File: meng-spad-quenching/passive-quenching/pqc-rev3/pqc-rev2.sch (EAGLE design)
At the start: 61 parts, among them IC1 OPA858, IC2 OPA858, IC4 TPS7A4901, X1 CONN_SPAD, X2 PWR, X4 VBIAS_IN, X5 SIGNAL_OUT

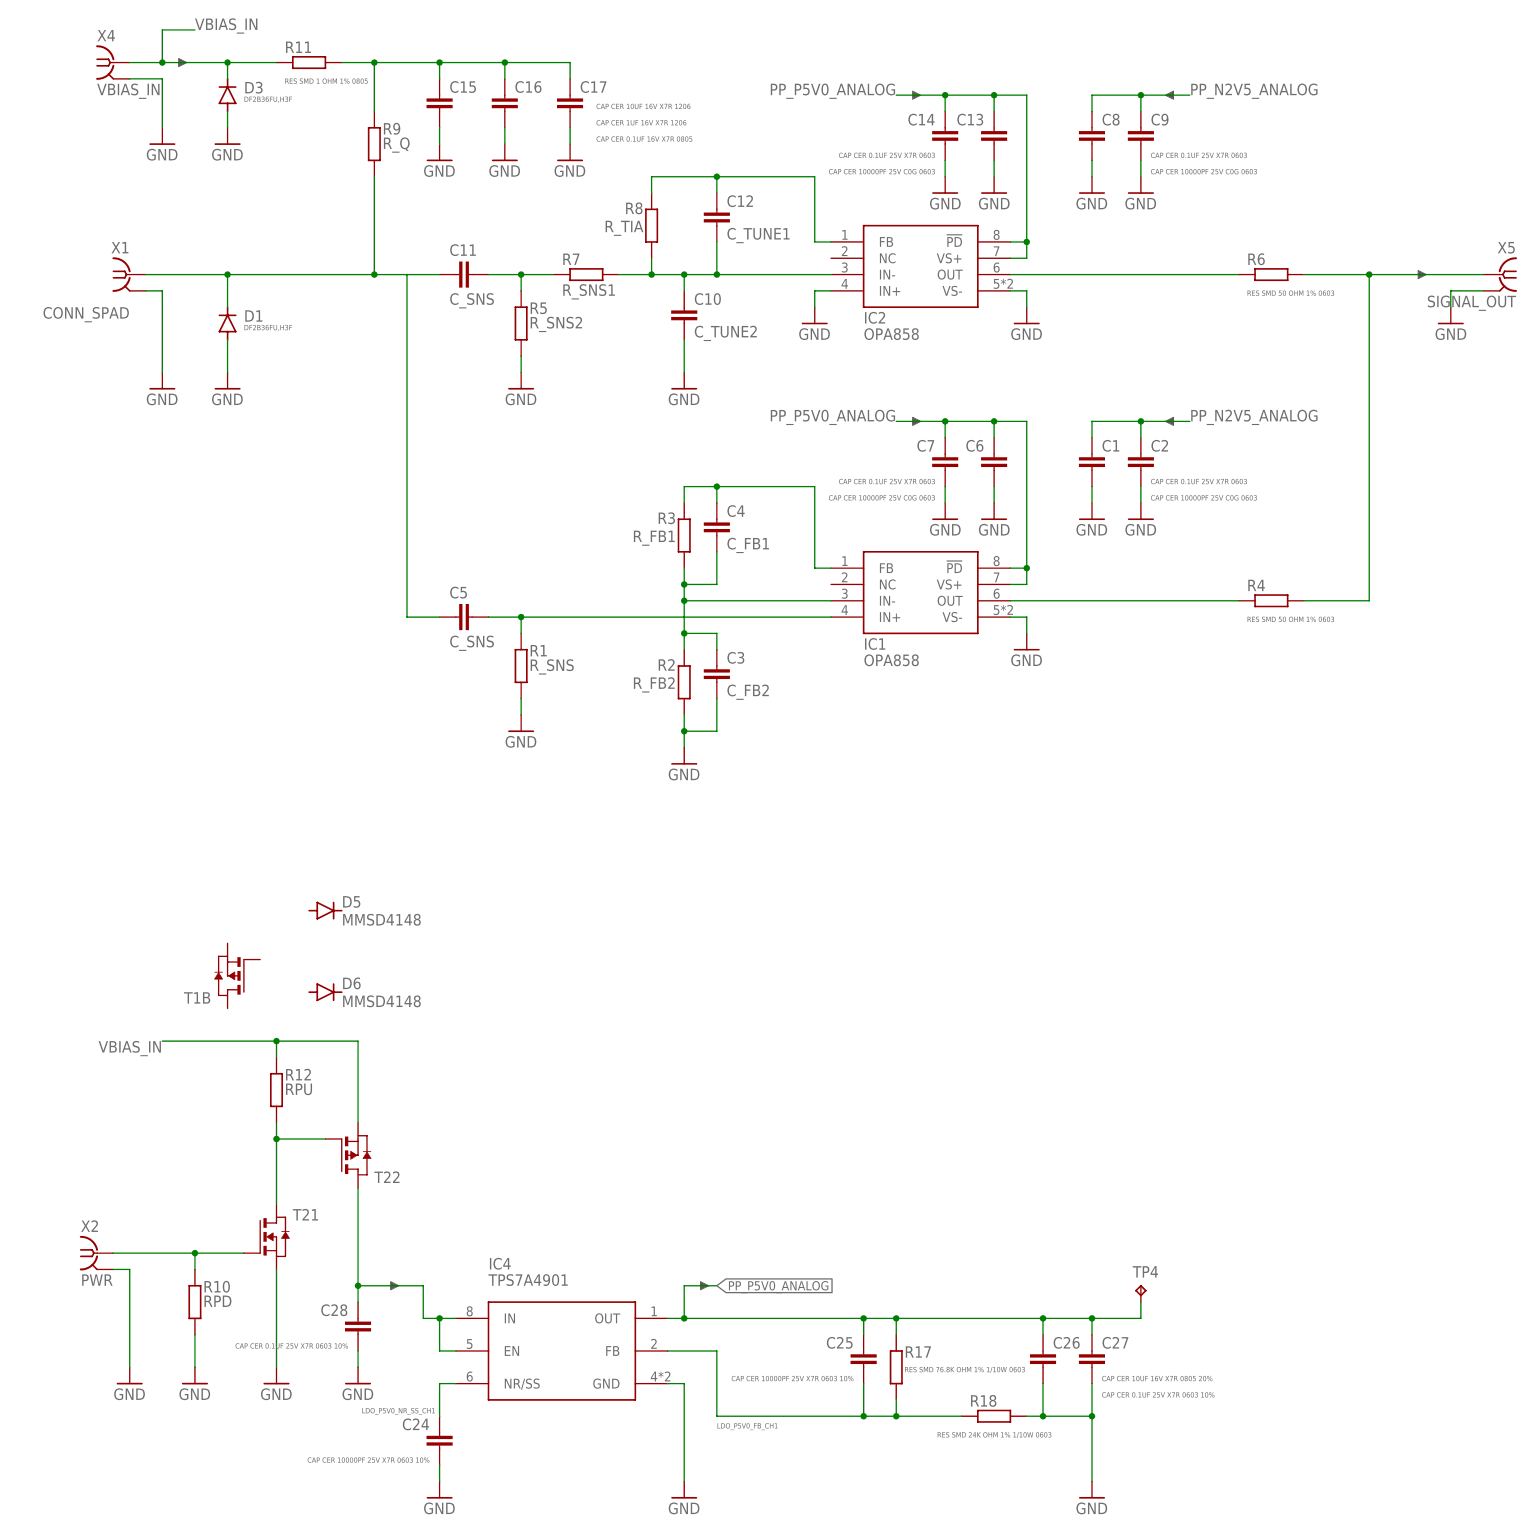
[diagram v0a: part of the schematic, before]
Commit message: Sim working with stand-ins for NMOS and PMOS switches
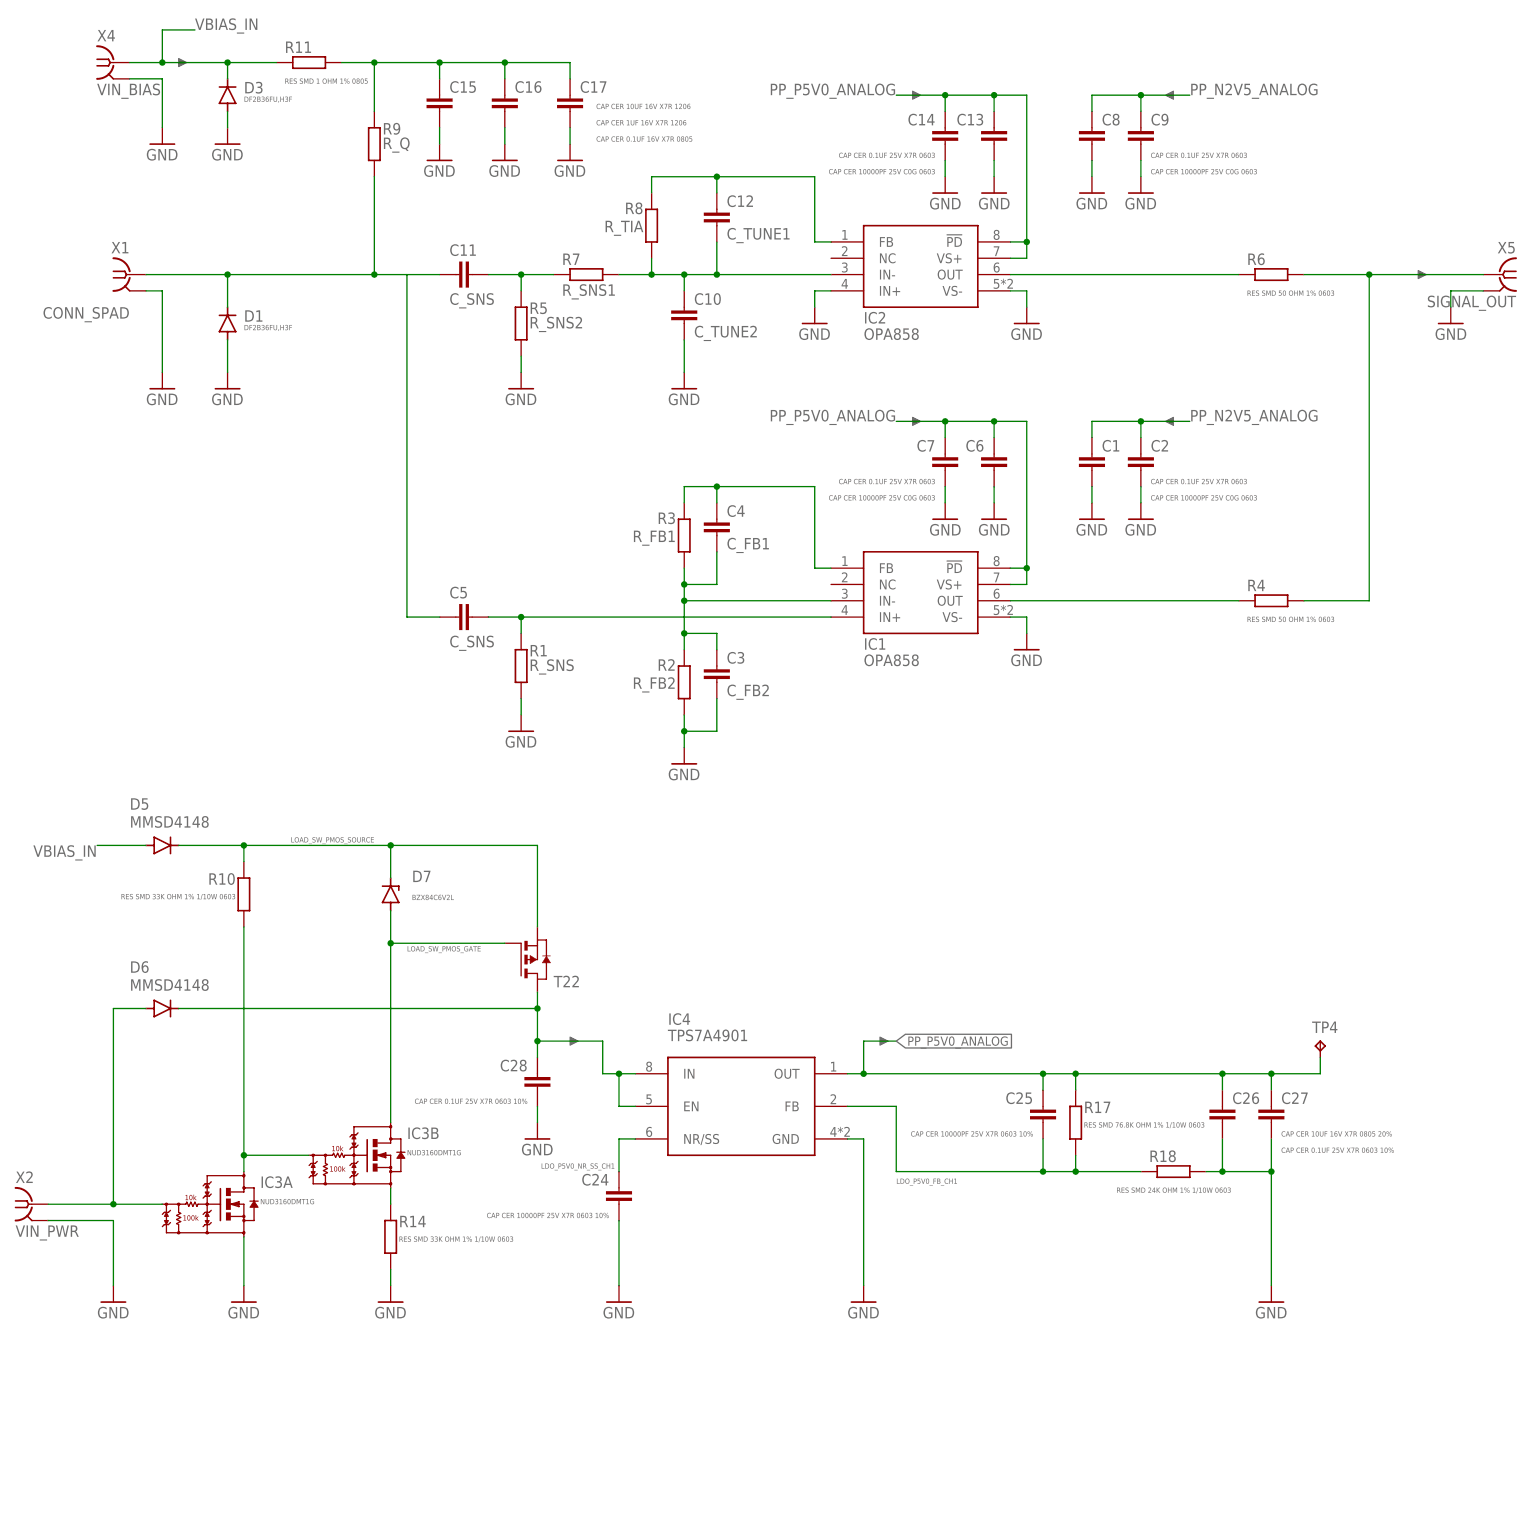
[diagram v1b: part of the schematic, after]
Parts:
- removed R12: RPU, rcl-modified-footprints:R-EU_R0402
- removed T1: (no value), zetex:PMOS2MSOP8
- added D7: BZX84C6V2L, diode:ZENER-DIODESOT23
- added IC3: NUD3160DMT1G, meng:NUD3160DMT1G
- added R14: RES SMD 33K OHM 1% 1/10W 0603, rcl-modified-footprints:R-EU_R0402
- R10: value RPD -> RES SMD 33K OHM 1% 1/10W 0603
- X2: value PWR -> VIN_PWR
- X4: value VBIAS_IN -> VIN_BIAS
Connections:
- removed net N$8: R12.1, T21.D, T22.G
- new net LOAD_SW_PMOS_GATE: D7.A, IC3B.D, T22.G
- new net LOAD_SW_PMOS_SOURCE: D5.C, D7.C, R10.2, T22.S
- new net N$14: D6.A, IC3A.G, X2COAX.1
- new net N$15: IC3B.S, R14.2
- net GND: now also IC3A.S, R14.1; no longer R10.1, T21.S
- net N$9: now also IC3A.D, IC3B.G, R10.1; no longer R10.2, T21.G, X2COAX.1
- net PP_P15V0_ANALOG: now also D6.C
- net VBIAS_IN: now also D5.A; no longer R12.2, T22.S
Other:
- note added: "Designed for 50V max. input"
- note added: "Limit upper clamp current"
- note added: "Prevent conduction through PMOS body diode"
- note added: "Todo: select PMOS device"
- note added: "VDS(max) = 61V"
- note removed: "Add gate protection network or pick load sw with prot"
- note removed: "Need gate voltage clamp"
- moved on the sheet: C24, C25, C26, C27, C28, D5, D6, IC4, R10, R17, R18, T22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

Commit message: 2 different power supply switching options investigated in sim
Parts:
- removed C1, C8: CAP CER 10000PF 25V C0G 0603, rcl-modified-footprints:C-EUC0603
- removed C2, C9: CAP CER 0.1UF 25V X7R 0603, rcl-modified-footprints:C-EUC0603
- removed C23: CAP CER 10UF 16V X7R 1206, rcl:C-EUC1206
- removed D2, D4: DF2B36FU,H3F, diode:DIODE-SOD323-W
- removed R13, R16: RES SMD 1 OHM 1% 0805, rcl-modified-footprints:R-EU_R0805
- removed T2: (no value), zetex:PN_MOSFET-MSOP8
- removed TP1: P2V5, testpad:TPTP20R
- removed TP2, TP4: GND, testpad:TPTP20R
- removed TP3: N2V5, testpad:TPTP20R
- added C20: CAP CER 0.1UF 100V X7R 0603, rcl-modified-footprints:C-EUC0603
- added Q1: NTR5105P, meng:PMOS_GENERIC_SOT23-3
- added Q2: BSS123LT1G, meng:NMOS_GENERIC
- added Q3: NUD3160LT1G, meng:NUD3160LT1G
- added R12: RES SMD 10M OHM 1% 1/10W 0603, rcl-modified-footprints:R-EU_R0402
- added R15: RES SMD 10K OHM 1% 1/10W 0603, rcl-modified-footprints:R-EU_R0402
- added R19, R20: RES SMD 1K OHM 1% 1/10W 0603, rcl-modified-footprints:R-EU_R0402
- C18, C19, C21: value CAP CER 10UF 16V X7R 1206 -> CAP CER 0.1UF 100V X7R 0603; device rcl:C-EUC1206 -> rcl-modified-footprints:C-EUC0603
- C28: value CAP CER 0.1UF 25V X7R 0603 10% -> CAP CER 0.1UF 100V X7R 0603
- IC3: value NUD3160DMT1G -> LM8261; device meng:NUD3160DMT1G -> meng:LM8261
- R10: value RES SMD 33K OHM 1% 1/10W 0603 -> RES SMD 10M OHM 1% 1/10W 0603; device rcl-modified-footprints:R-EU_R0402 -> rcl-modified-footprints:R-EU_R0603
- R14: value RES SMD 33K OHM 1% 1/10W 0603 -> RES SMD 10K OHM 1% 1/10W 0603
- R9: device rcl:R-EU_R0805 -> rcl:R-EU_R0603
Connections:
- removed net N$14: D6.A, IC3A.G, X2COAX.1
- removed net N$15: IC3B.S, R14.2
- removed net N$9: IC3A.D, IC3B.G, R10.1
- removed net PP_N2V5_ANALOG: C1.1, C18.1, C2.1, C8.1, C9.1, TP3.TP
- removed net PP_NVIN: C23.1, D2.C, R13.1
- removed net PP_NVIN_CONN: R13.2
- removed net PP_P15V0_ANALOG: C28.1, D6.C, IC4.EN, IC4.IN, T22.D
- removed net PP_P2V5_ANALOG: C19.1, TP1.TP
- removed net PP_PVIN: C21.1, D4.C, R16.1
- removed net PP_PVIN_CONN: R16.2
- new net LDO_IN: C28.1, D6.C, IC4.EN, IC4.IN, Q1.D
- new net LOAD_SW_NMOS_DRAIN: Q2.D, R15.1
- new net LOAD_SW_NMOS_GATE: Q2.G, Q3.D, R10.1
- new net LOAD_SW_NMOS_SOURCE: Q2.S, R14.2
- new net N$17: C18.1, IC3.+IN, R19.1, R20.2
- new net VPWR_IN: D6.A, Q3.G, X2COAX.1
- new net VREF_2V5: C10.2, C20.1, C21.1, C3.2, IC3.-IN, IC3.OUT, R1.1, R2.2, R5.1
- net GND: now also C20.2, IC3.V-, Q3.S, R20.1; no longer C1.2, C10.2, C2.2, C23.2, C3.2, C8.2, C9.2, D2.A, D4.A, IC3A.S, R1.1, R2.2, R5.1, TP2.TP
- net LOAD_SW_PMOS_GATE: now also Q1.G, R12.1, R15.2; no longer IC3B.D, T22.G
- net LOAD_SW_PMOS_SOURCE: now also Q1.S, R12.2; no longer T22.S
- net PP_P5V0_ANALOG: now also C19.1, IC3.V+, R19.2; no longer TP4.TP
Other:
- note added: "100mA output current limit"
- note added: "ESD Update MPN for 50V"
- note added: "Midrail reference buffer"
- note added: "OPA858: 20.5mA Iq LM8261: 1.0mA Iq Ref divider: 2.5mA Iq Total: 24.0mA Iq +Output current into load 2.5V Vq into 50R(src)+50R(load) is 25mA 50mA * 50V = 2.5W (!!!)"
- note added: "Prevent conduction through PMOS body diode Package = SOD123"
- note added: "This package pinout works for various MSOP8 Power Pad high-voltage LDOs. Checked: LT3010-5 (10k-100k = 100uVrms noise) TPS79850 (10k-100k = 100uVrms noise)"
- note added: "VDS(max) = 100V IGSS = 50nA"
- note added: "VDS(max) = 60V"
- note added: "VGS +/-20V rated"
- note removed: "All feedback resistors 1%"
- note removed: "ESD"
- note removed: "OPA858: 20.5mA Iq"
- note removed: "Prevent conduction through PMOS body diode"
- note removed: "Todo: select PMOS device"
- note removed: "VDS(max) = 61V"
- moved on the sheet: C18, C19, C21, D5, D6, D7, R10, R14, R18, R4, R6, X2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

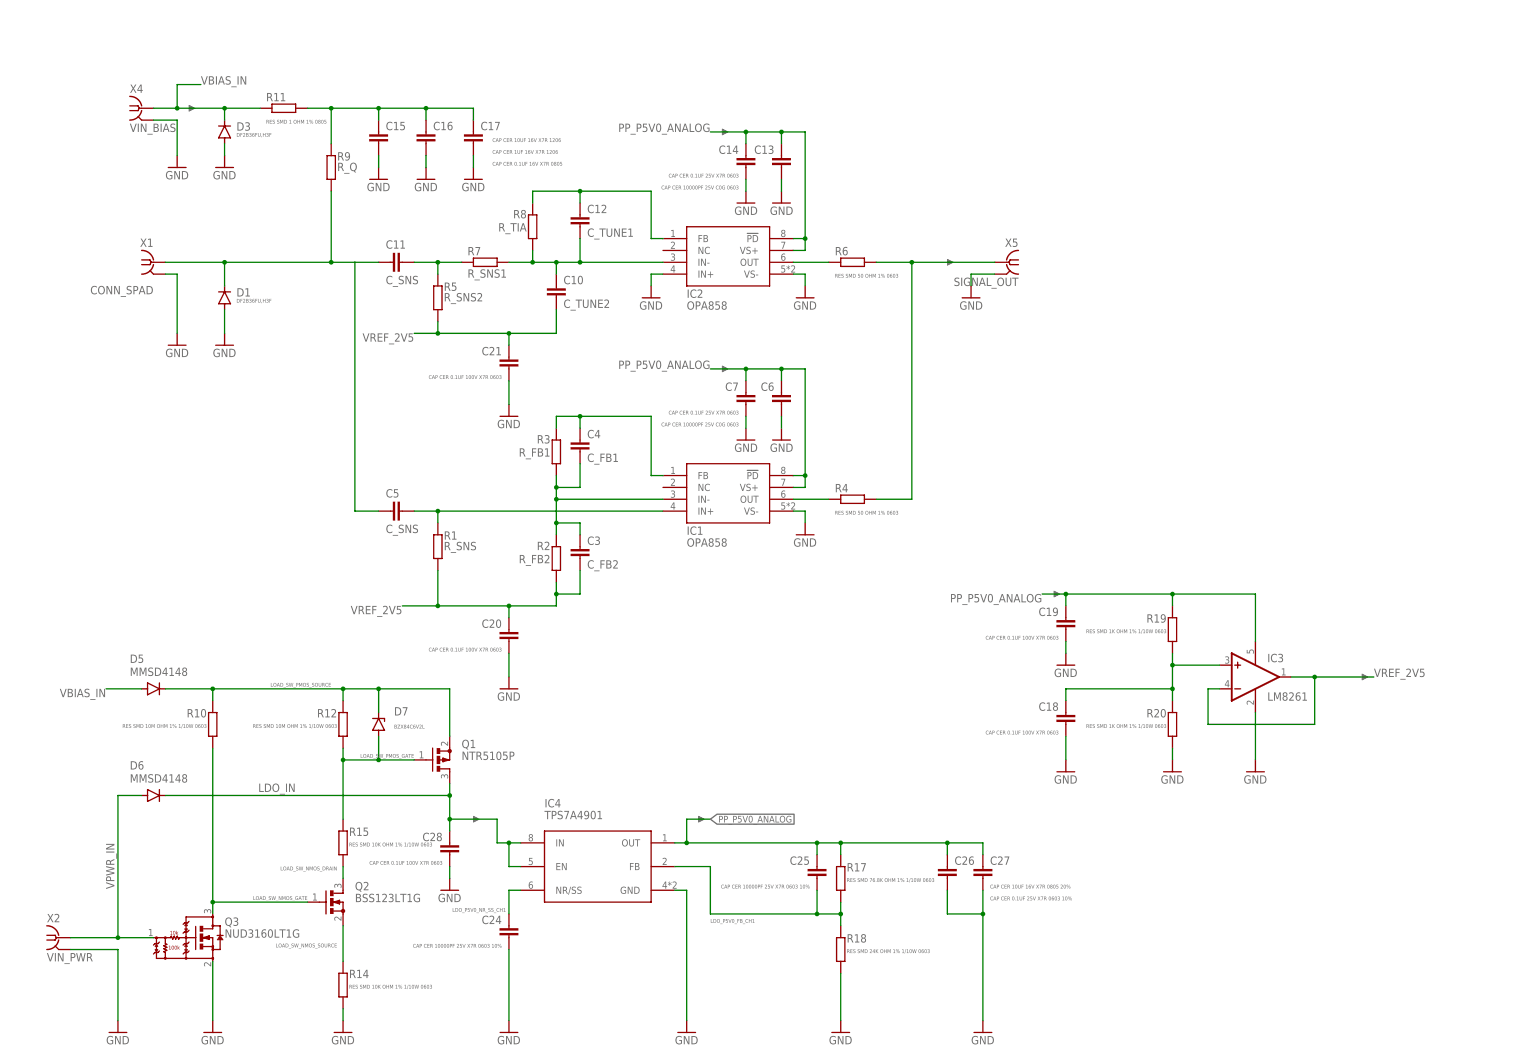
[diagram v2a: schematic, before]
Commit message: Everything fits on board, placement still preliminary
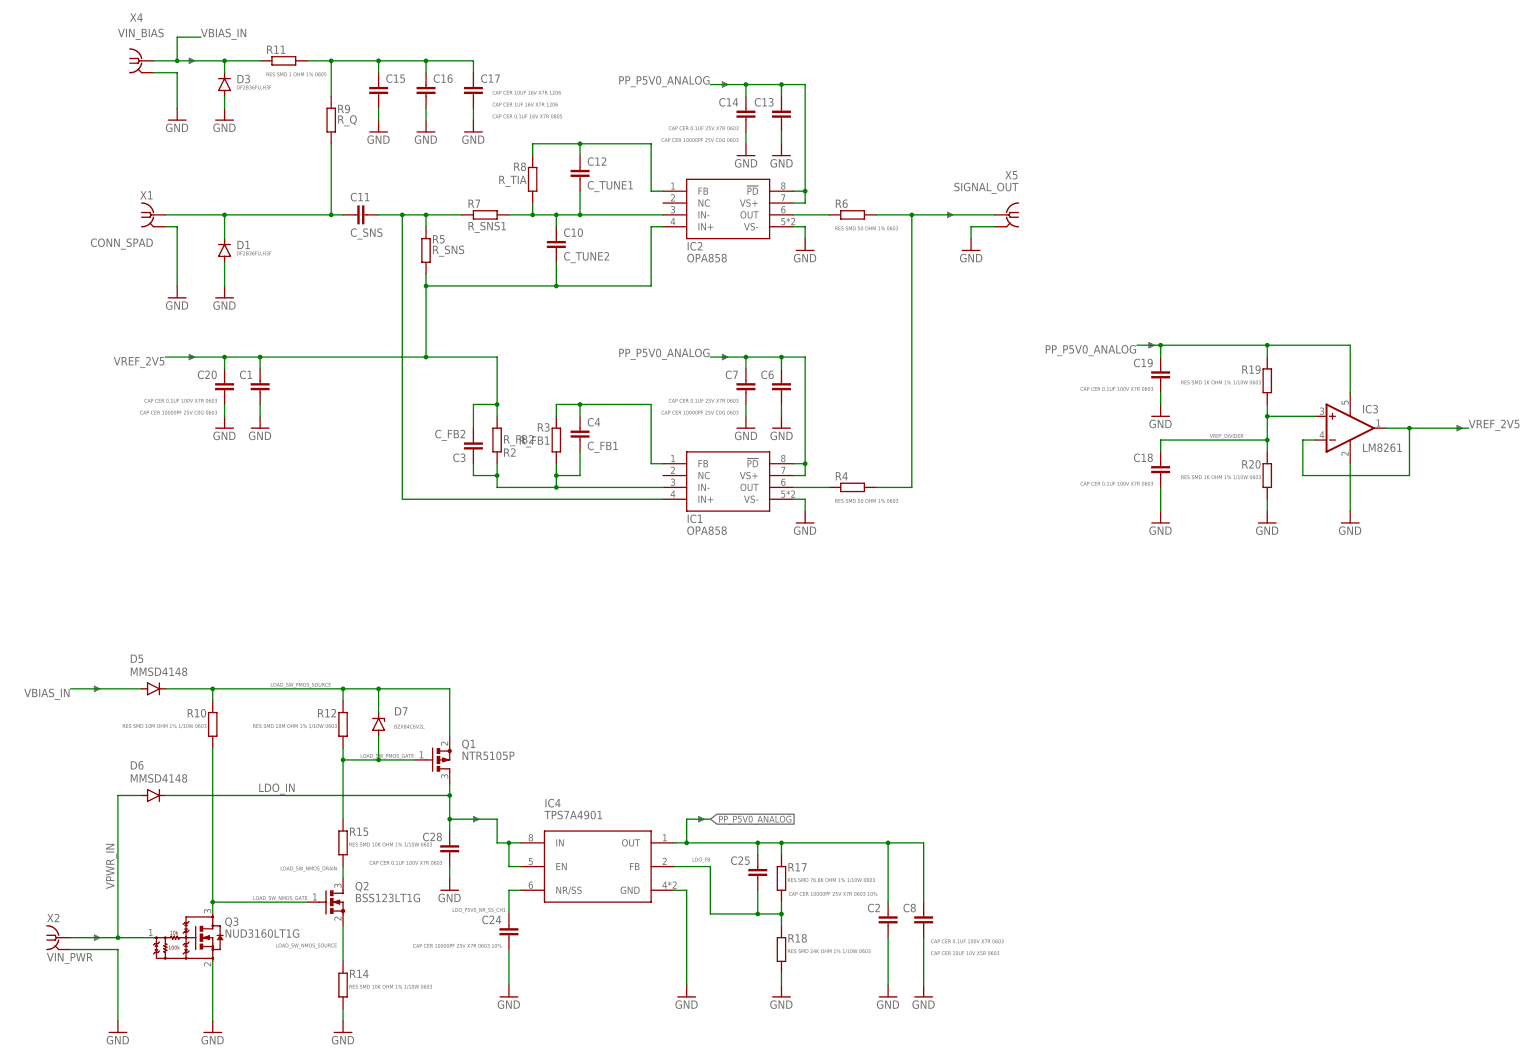
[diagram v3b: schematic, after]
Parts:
- removed C21: CAP CER 0.1UF 100V X7R 0603, rcl-modified-footprints:C-EUC0603
- removed C26: CAP CER 0.1UF 25V X7R 0603 10%, rcl-modified-footprints:C-EUC0603
- removed C27: CAP CER 10UF 16V X7R 0805 20%, rcl:C-EUC0805
- removed C5: C_SNS, rcl-modified-footprints:C-EUC0603
- removed R1: R_SNS, rcl-modified-footprints:R-EU_R0402
- added C1: CAP CER 10000PF 25V C0G 0603, rcl-modified-footprints:C-EUC0603
- added C2: CAP CER 0.1UF 100V X7R 0603, rcl-modified-footprints:C-EUC0603
- added C8: CAP CER 10UF 10V X5R 0603, rcl-modified-footprints:C-EUC0603
- R12, R14, R15, R19, R20: device rcl-modified-footprints:R-EU_R0402 -> rcl-modified-footprints:R-EU_R0603
- R5: value R_SNS2 -> R_SNS
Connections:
- net LDO_P5V0_FB_CH1 renamed LDO_FB
- net N$17 renamed VREF_DIVIDER
- removed net N$3: C11.2, R5.2, R7.2
- net GND: now also C1.2, C2.2, C8.2; no longer C21.2, C26.2, C27.2, IC2.IN+
- net N$2: no longer C5.1
- net N$6: now also C11.2, R5.2, R7.2; no longer C5.2, R1.2
- net PP_P5V0_ANALOG: now also C2.1, C8.1; no longer C26.1, C27.1
- net VREF_2V5: now also C1.1, IC2.IN+; no longer C21.1, R1.1
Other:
- moved on the sheet: C10, C11, C12, C13, C14, C15, C16, C17, C18, C19, C20, C25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
